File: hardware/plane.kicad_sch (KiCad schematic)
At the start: 21 parts, among them J1 USB_B_Micro, Q1 BSS138, Q2 BSS138, U1 ESP32-WROOM-32, U2 AMS1117-3.3, U3 CH340C

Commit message: add lora
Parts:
- removed D1: LED, LED_SMD:LED_0603_1608Metric, symbol Device:LED
- removed R6: R_Small, Resistor_SMD:R_0603_1608Metric, symbol Device:R_Small
- added C6: C, Capacitor_SMD:C_0603_1608Metric, symbol Device:C
- added J2: Conn_Coaxial, symbol Connector:Conn_Coaxial
- added U4: RFM95W-868S2, symbol RF_Module:RFM95W-868S2
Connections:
- net +3V3: now also C6.1, U4.13 (3.3V)
- net GND: now also C6.2, J2.2 (Ext), U4.1 (GND), U4.10 (GND), U4.8 (GND)
- net MOSI: now reaches U1.16 (IO13)
- net MOSI: now also U4.3 (MOSI)
- net SCLK: now reaches U1.13 (IO14)
- net SCLK: now also U4.4 (SCK)
- net at R5.1: now also U1.37 (IO23); no longer U1.14 (IO12)
- net SS: now reaches U1.23 (IO15)
- net SS: now also U4.5 (NSS)
- net LORA_RST: now reaches U1.27 (IO16)
- net LORA_RST: now also U4.6 (RESET)
- net DIO0: now reaches U1.28 (IO17)
- net DIO0: now also U4.14 (DIO0)
- net DIO1: now reaches U1.30 (IO18)
- net DIO1: now also U4.15 (DIO1)
- net DIO2: now reaches U1.31 (IO19)
- net DIO2: now also U4.16 (DIO2)
- new net: J2.1 (In), U4.9 (ANT)
- new net MISO: U1.14 (IO12), U4.2 (MISO)
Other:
- moved on the sheet: D2, R2, R3, R5

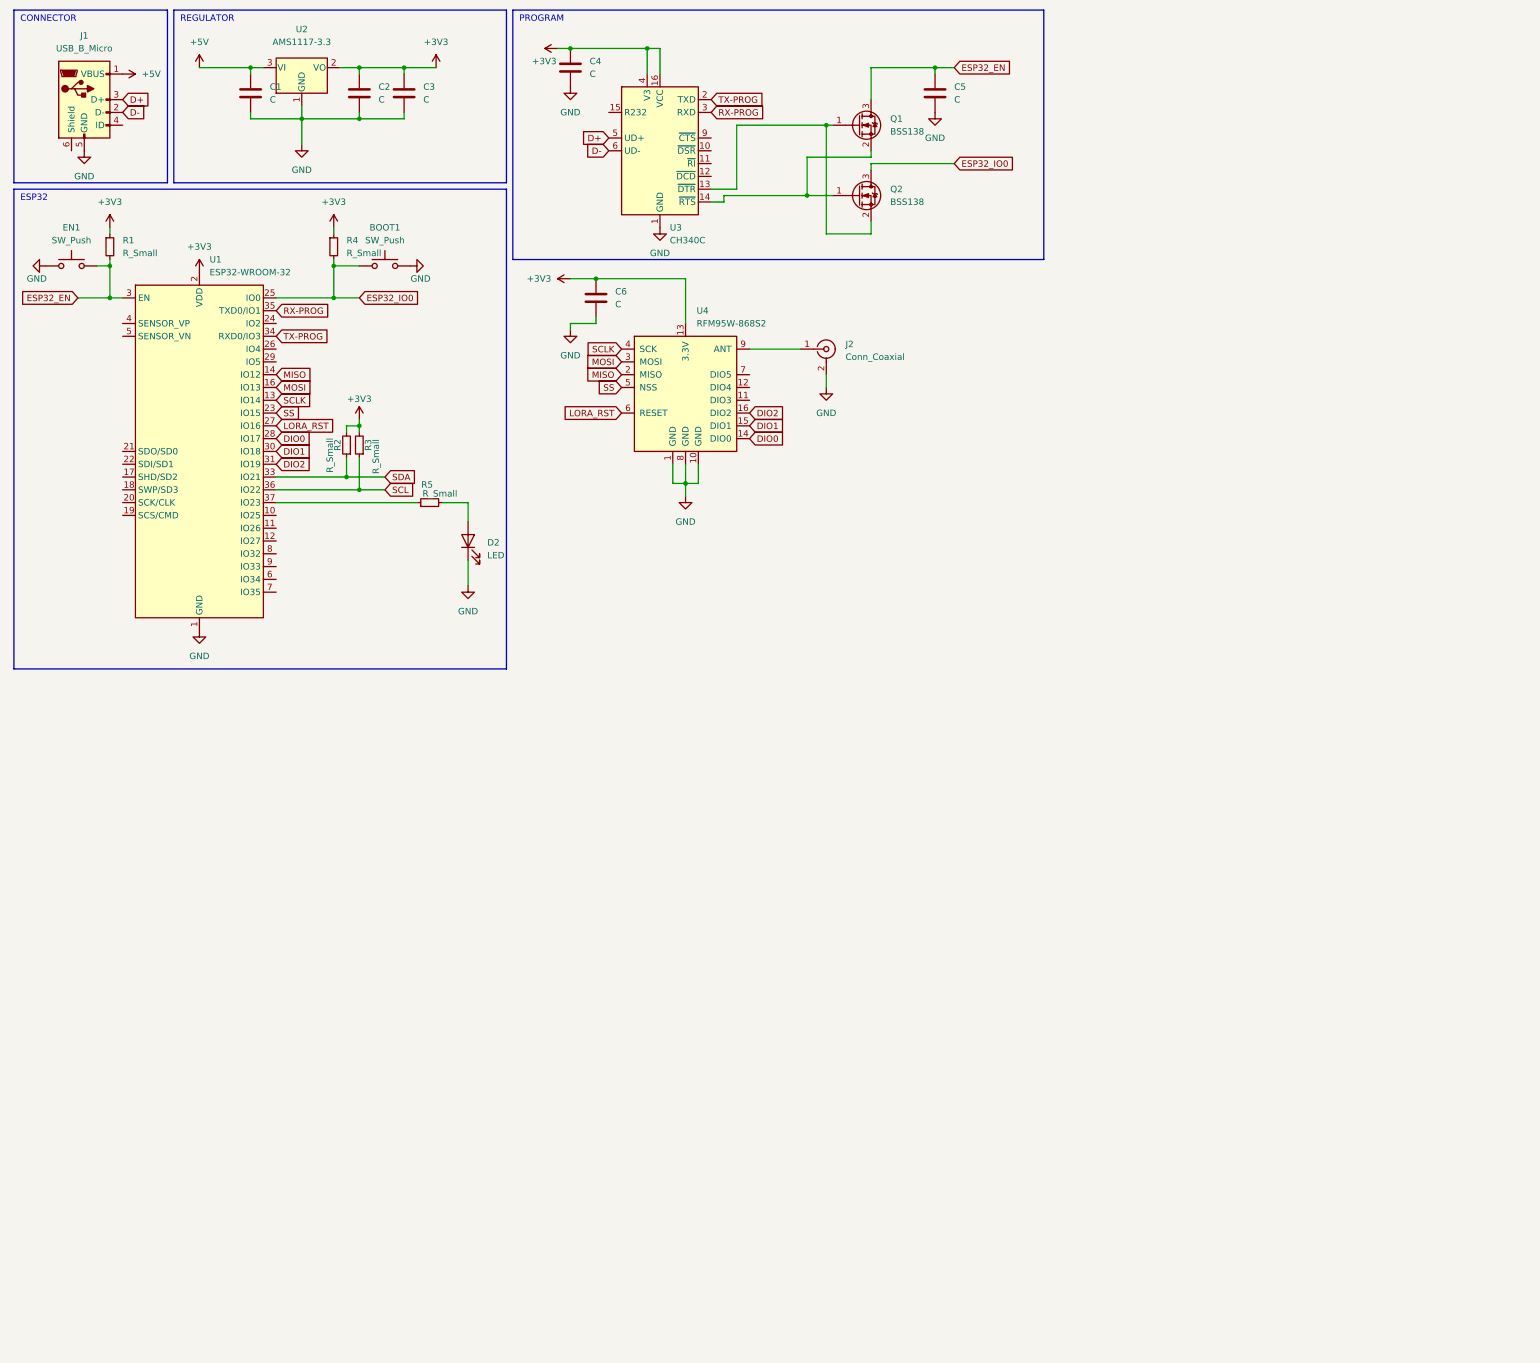
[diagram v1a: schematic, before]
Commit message: add mpu + bmp
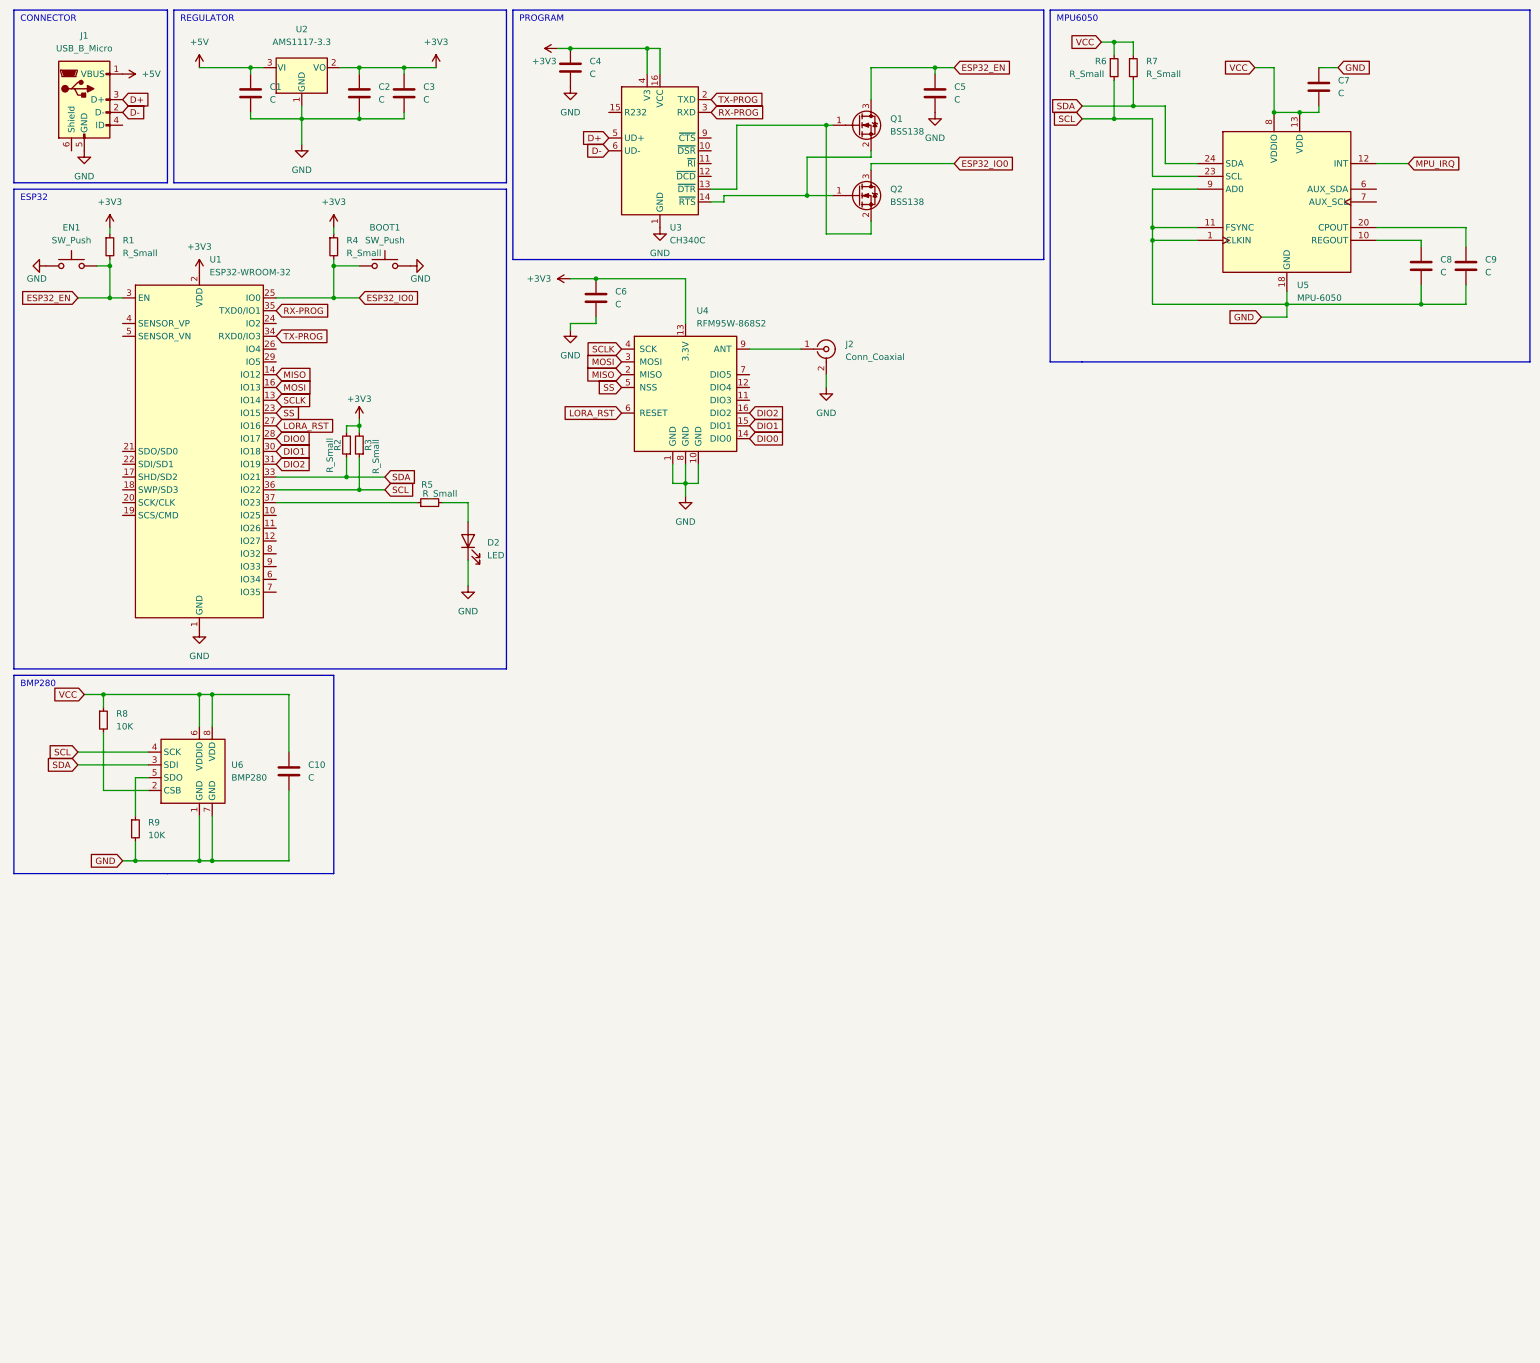
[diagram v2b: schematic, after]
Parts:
- added C10, C7, C8, C9: C, Capacitor_SMD:C_0603_1608Metric, symbol Device:C
- added R6, R7: R_Small, Resistor_SMD:R_0603_1608Metric, symbol Device:R_Small
- added R8, R9: 10K, Resistor_SMD:R_0603_1608Metric, symbol Device:R_Small
- added U5: MPU-6050, Sensor_Motion:InvenSense_QFN-24_4x4mm_P0.5mm, symbol Sensor_Motion:MPU-6050
- added U6: BMP280, Package_LGA:Bosch_LGA-8_2x2.5mm_P0.65mm_ClockwisePinNumbering, symbol Sensor_Pressure:BMP280
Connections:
- net GND: now also C10.2, C7.1, C8.2, C9.2, R9.2, U5.1 (CLKIN), U5.11 (FSYNC), U5.18 (GND), U5.9 (AD0), U6.1 (GND), U6.7 (GND)
- net SCL: now also R6.2, U5.23 (SCL), U6.4 (SCK)
- net SDA: now also R7.2, U5.24 (SDA), U6.3 (SDI)
- new net: R9.1, U6.5 (SDO)
- new net: R8.2, U6.2 (CSB)
- new net: C9.1, U5.20 (CPOUT)
- new net: C8.1, U5.10 (REGOUT)
- new net MPU_IRQ: U5.12 (INT)
- new net VCC: C10.1, C7.2, R6.1, R7.1, R8.1, U5.13 (VDD), U5.8 (VDDIO), U6.6 (VDDIO), U6.8 (VDD)
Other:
- note added: "BMP280"
- note added: "MPU6050"

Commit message: add footprints
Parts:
- J2: footprint (none) -> Connector_Coaxial:SMA_Amphenol_132289_EdgeMount
- U4: footprint (none) -> RF_Module:HOPERF_RFM9XW_SMD
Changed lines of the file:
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@@
 			)
 		)
-		(property "Footprint" ""
+		(property "Footprint" "Connector_Coaxial:SMA_Amphenol_132289_EdgeMount"
 			(at 173.99 80.01 0)
 			(effects
@@
 			)
 		)
-		(property "Footprint" ""
+		(property "Footprint" "RF_Module:HOPERF_RFM9XW_SMD"
 			(at 62.23 45.72 0)
 			(effects

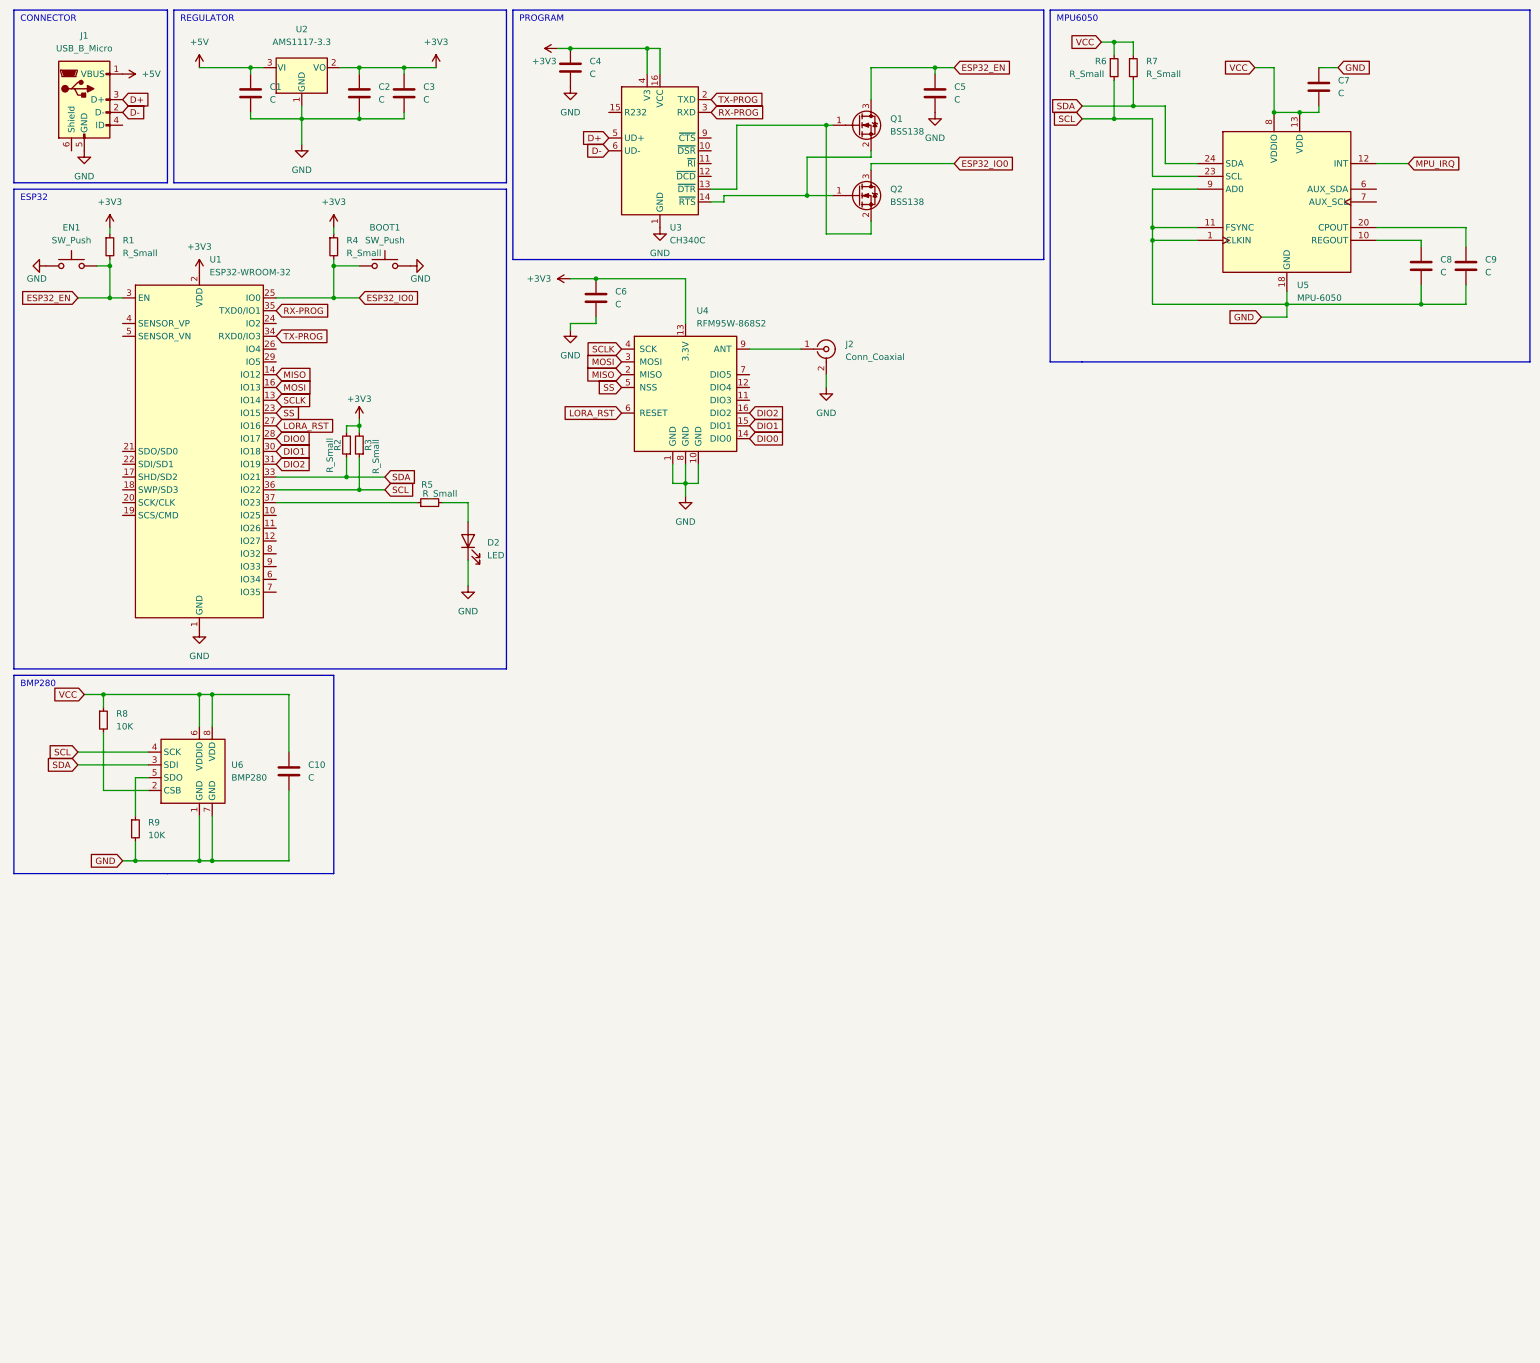
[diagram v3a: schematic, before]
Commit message: add servos + pcb size
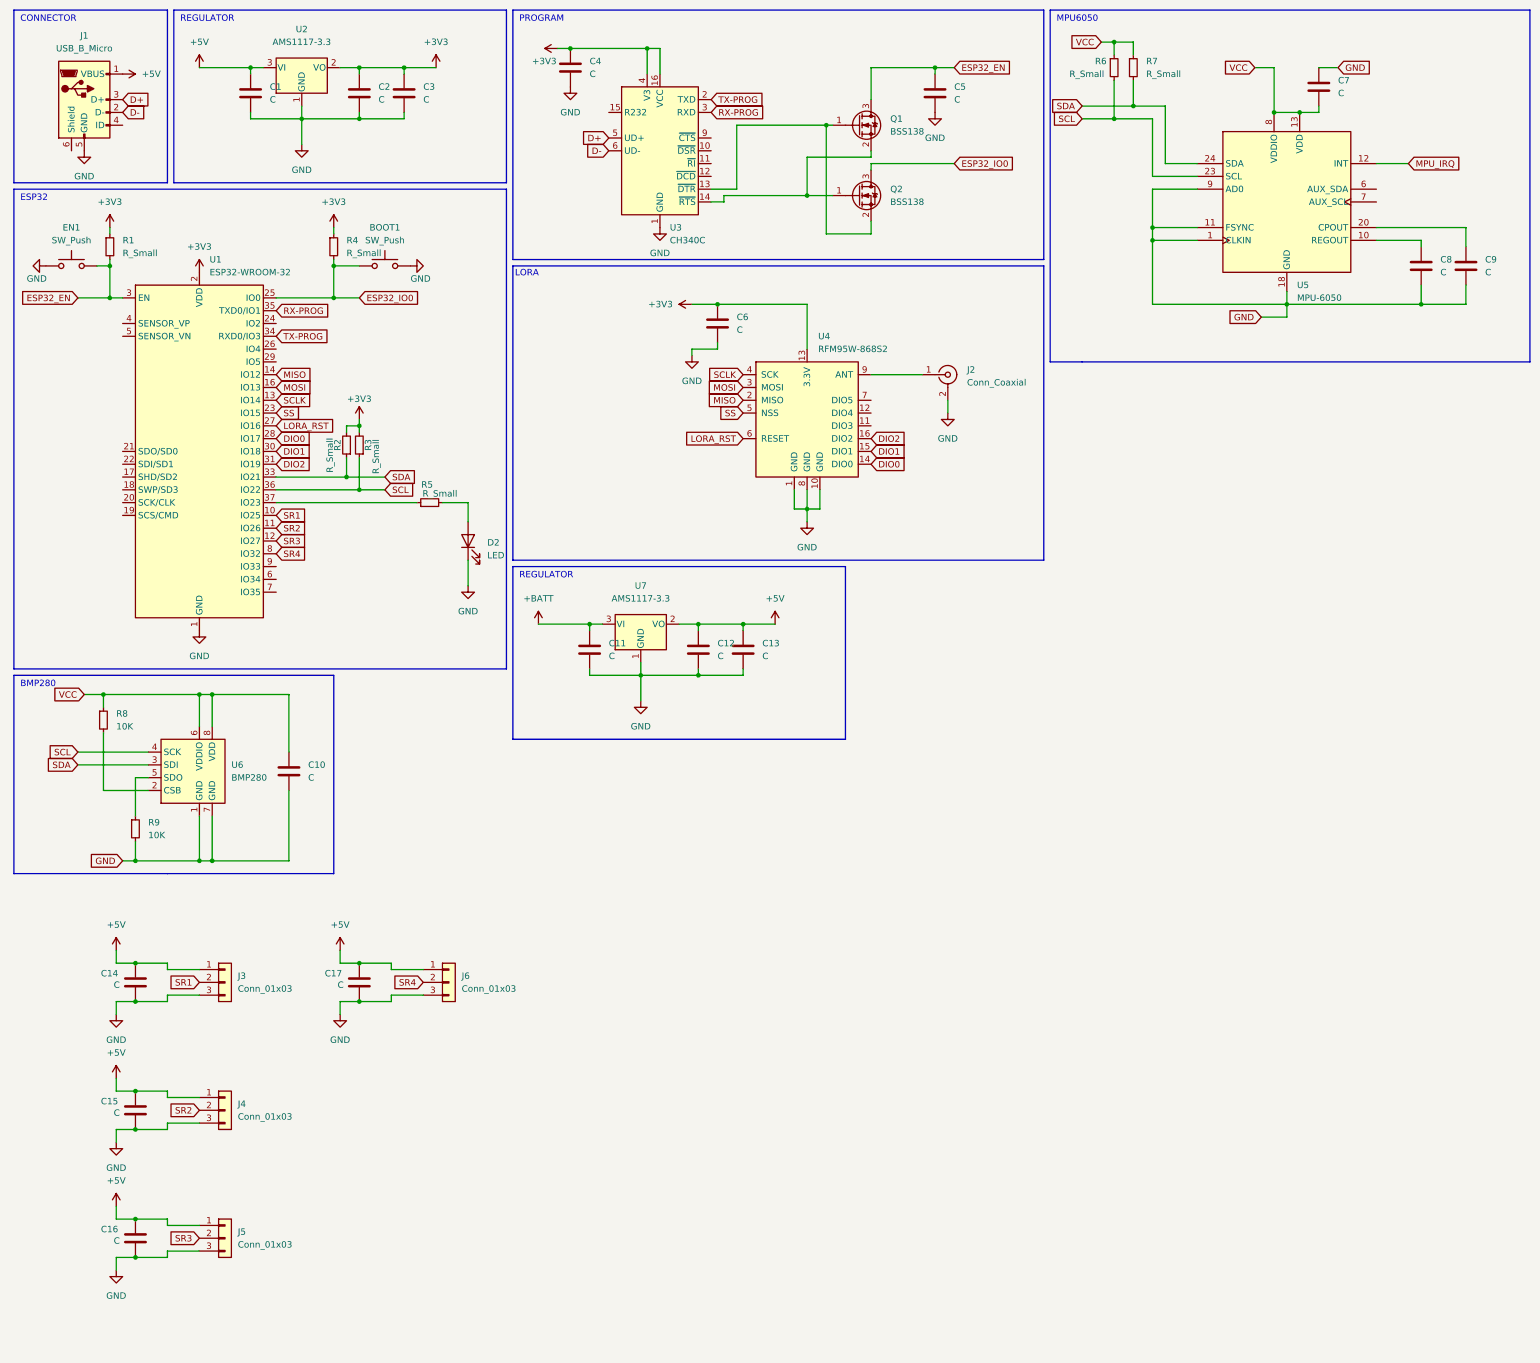
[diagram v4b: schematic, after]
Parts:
- added C11, C12, C13, C14, C15, C16, C17: C, Capacitor_SMD:C_0603_1608Metric, symbol Device:C
- added J3, J4, J5, J6: Conn_01x03, symbol Connector_Generic:Conn_01x03
- added U7: AMS1117-3.3, Package_TO_SOT_SMD:SOT-223-3_TabPin2, symbol Regulator_Linear:AMS1117-3.3
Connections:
- net +5V: now also C12.1, C13.1, C14.1, C15.1, C16.1, C17.1, J3.1 (Pin_1), J4.1 (Pin_1), J5.1 (Pin_1), J6.1 (Pin_1), U7.2 (VO)
- net GND: now also C11.2, C12.2, C13.2, C14.2, C15.2, C16.2, C17.2, J3.3 (Pin_3), J4.3 (Pin_3), J5.3 (Pin_3), J6.3 (Pin_3), U7.1 (GND)
- net SR1: now reaches U1.10 (IO25)
- net SR1: now also J3.2 (Pin_2)
- net SR2: now reaches U1.11 (IO26)
- net SR2: now also J4.2 (Pin_2)
- net SR3: now reaches U1.12 (IO27)
- net SR3: now also J5.2 (Pin_2)
- net SR4: now reaches U1.8 (IO32)
- net SR4: now also J6.2 (Pin_2)
- new net +BATT: C11.1, U7.3 (VI)
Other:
- note added: "LORA"
- moved on the sheet: C6, J2, U4
